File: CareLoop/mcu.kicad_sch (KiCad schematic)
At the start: 26 parts, among them J1_DEBUG1 Conn_01x04_Pin, U6 nRF52840-QFXX, Y1 32MHz, Y2 32.768kHz

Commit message: update PCB
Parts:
- C1, C2, C3, C4: JLCPCB Part#(optional) (none) -> C107034
- C10, C9: JLCPCB Part#(optional) (none) -> C62550
- C11, C7: JLCPCB Part#(optional) (none) -> C88945
- C12: JLCPCB Part#(optional) (none) -> C161494
- C5: JLCPCB Part#(optional) (none) -> C172832
- C6: JLCPCB Part#(optional) (none) -> C50388
- C8: JLCPCB Part#(optional) (none) -> C85925
- D3: JLCPCB Part#(optional) (none) -> C20608782
- J1_DEBUG1: footprint Connector_PinHeader_1.00mm:PinHeader_1x04_P1.00mm_Vertical -> Connector_PinHeader_2.00mm:PinHeader_1x04_P2.00mm_Vertical; now not fitted
- L1: JLCPCB Part#(optional) (none) -> C2043482
- L2: JLCPCB Part#(optional) (none) -> C2047913
- L5: JLCPCB Part#(optional) (none) -> C1035
- L6: JLCPCB Part#(optional) (none) -> C81212
- R1: JLCPCB Part#(optional) (none) -> C25531
- R2, R3: JLCPCB Part#(optional) (none) -> C22369185
- R4: JLCPCB Part#(optional) (none) -> C25097
- Reset_SW1: JLCPCB Part#(optional) (none) -> C2733655
- U6: JLCPCB Part#(optional) (none) -> C9900145907
- Y1: JLCPCB Part#(optional) (none) -> C252280
- Y2: JLCPCB Part#(optional) (none) -> C2449817
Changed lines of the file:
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@@
+			)
+		)
+		(property "JLCPCB Part#(optional)" "C161494"
+			(at 90.17 26.67 90)
+			(effects
+				(font
+					(size 1.27 1.27)
+				)
+				(hide yes)
 			)
 		)
@@
 			)
 		)
+		(property "JLCPCB Part#(optional)" "C9900145907"
+			(at 96.52 104.14 0)
+			(effects
+				(font
+					(size 1.27 1.27)
+				)
+				(hide yes)
+			)
+		)
 		(pin "35"
 		)
@@
 			)
 		)
+		(property "JLCPCB Part#(optional)" "C2449817"
+			(at 54.61 76.2 90)
+			(effects
+				(font
+					(size 1.27 1.27)
+				)
+				(hide yes)
+			)
+		)
 		(pin "1"
 		)
@@
 		(property "Description" "Resistor"
 			(at 45.72 127 0)
+			(effects
+				(font
+					(size 1.27 1.27)
+				)
+				(hide yes)
+			)
+		)
+		(property "JLCPCB Part#(optional)" "C25097"
+			(at 45.72 127 90)
 			(effects
 				(font
@@
 			)
 		)
+		(property "JLCPCB Part#(optional)" "C50388"
+			(at 160.02 100.33 0)
+			(effects
+				(font
+					(size 1.27 1.27)
+				)
+				(hide yes)
+			)
+		)
 		(pin "1"
 		)
@@
 		)
 		(property "Description" "Unpolarized capacitor, small symbol"
+			(at 139.7 55.88 0)
+			(effects
+				(font
+					(size 1.27 1.27)
+				)
+				(hide yes)
+			)
+		)
+		(property "JLCPCB Part#(optional)" "C62550"
 			(at 139.7 55.88 0)
 			(effects
@@
 			)
 		)
+		(property "JLCPCB Part#(optional)" "C81212"
+			(at 118.11 36.83 90)
+			(effects
+				(font
+					(size 1.27 1.27)
+				)
+				(hide yes)
+			)
+		)
 		(pin "2"
 		)
@@
 			)
 		)
+		(property "JLCPCB Part#(optional)" "C107034"
+			(at 45.72 80.01 90)
+			(effects
+				(font
+					(size 1.27 1.27)
+				)
+				(hide yes)
+			)
+		)
 		(pin "2"
 		)
@@
 			)
 		)
+		(property "JLCPCB Part#(optional)" "C2733655"
+			(at 148.59 147.32 0)
+			(effects
+				(font
+					(size 1.27 1.27)
+				)
+				(hide yes)
+			)
+		)
 		(pin "1"
 		)
@@
 		(property "Description" "Unpolarized capacitor, small symbol"
 			(at 45.72 72.39 0)
+			(effects
+				(font
+					(size 1.27 1.27)
+				)
+				(hide yes)
+			)
+		)
+		(property "JLCPCB Part#(optional)" "C107034"
+			(at 45.72 72.39 90)
 			(effects
 				(font
@@
 			)
 		)
+		(property "JLCPCB Part#(optional)" "C2047913"
+			(at 154.94 104.14 90)
+			(effects
+				(font
+					(size 1.27 1.27)
+				)
+				(hide yes)
+			)
+		)
 		(pin "2"
 		)
@@
 			)
 		)
+		(property "JLCPCB Part#(optional)" "C2043482"
+			(at 165.1 104.14 90)
+			(effects
+				(font
+					(size 1.27 1.27)
+				)
+				(hide yes)
+			)
+		)
 		(pin "2"
 		)
@@
 			)
 		)
+		(property "JLCPCB Part#(optional)" "C85925"
+			(at 144.78 68.58 0)
+			(effects
+				(font
+					(size 1.27 1.27)
+				)
+				(hide yes)
+			)
+		)
 		(pin "2"
 		)
@@
 		(property "Description" "Unpolarized capacitor, small symbol"
 			(at 45.72 64.77 0)
+			(effects
+				(font
+					(size 1.27 1.27)
+				)
+				(hide yes)
+			)
+		)
+		(property "JLCPCB Part#(optional)" "C107034"
+			(at 45.72 64.77 90)
 			(effects
 				(font
@@
 			)
 		)
+		(property "JLCPCB Part#(optional)" "C172832"
+			(at 149.86 100.33 0)
+			(effects
+				(font
+					(size 1.27 1.27)
+				)
+				(hide yes)
+			)
+		)
 		(pin "1"
 		)
@@
 			)
 		)
+		(property "JLCPCB Part#(optional)" "C88945"
+			(at 134.62 68.58 0)
+			(effects
+				(font
+					(size 1.27 1.27)
+				)
+				(hide yes)
+			)
+		)
 		(pin "2"
 		)
@@
 			)
 		)
+		(property "JLCPCB Part#(optional)" "C252280"
+			(at 57.15 60.96 90)
+			(effects
+				(font
+					(size 1.27 1.27)
+				)
+				(hide yes)
+			)
+		)
 		(pin "1"
 		)
@@
 			)
 		)
+		(property "JLCPCB Part#(optional)" "C88945"
+			(at 90.17 36.83 90)
+			(effects
+				(font
+					(size 1.27 1.27)
+				)
+				(hide yes)
+			)
+		)
 		(pin "2"
 		)
@@
 			)
 		)
+		(property "JLCPCB Part#(optional)" "C22369185"
+			(at 139.7 116.84 0)
+			(effects
+				(font
+					(size 1.27 1.27)
+				)
+				(hide yes)
+			)
+		)
 		(pin "1"
 		)
@@
 			)
 		)
+		(property "JLCPCB Part#(optional)" "C107034"
+			(at 45.72 57.15 90)
+			(effects
+				(font
+					(size 1.27 1.27)
+				)
+				(hide yes)
+			)
+		)
 		(pin "1"
 		)
@@
 		(in_bom yes)
 		(on_board yes)
-		(dnp no)
+		(dnp yes)
 		(property "Reference" "J1_DEBUG1"
 			(at 139.7 162.56 90)
@@
 			)
 		)
-		(property "Footprint" "Connector_PinHeader_1.00mm:PinHeader_1x04_P1.00mm_Vertical"
+		(property "Footprint" "Connector_PinHeader_2.00mm:PinHeader_1x04_P2.00mm_Vertical"
 			(at 138.43 160.02 0)
 			(effects
@@
 		(property "Description" "Generic connector, single row, 01x04, script generated"
 			(at 138.43 160.02 0)
+			(effects
+				(font
+					(size 1.27 1.27)
+				)
+				(hide yes)
+			)
+		)
+		(property "JLCPCB Part#(optional)" ""
+			(at 138.43 160.02 90)
 			(effects
 				(font
@@
 			)
 		)
+		(property "JLCPCB Part#(optional)" "C20608782"
+			(at 36.83 129.54 90)
+			(effects
+				(font
+					(size 1.27 1.27)
+				)
+				(hide yes)
+			)
+		)
 		(pin "2"
 		)
@@
 			)
 		)
+		(property "JLCPCB Part#(optional)" "C22369185"
+			(at 133.35 121.92 0)
+			(effects
+				(font
+					(size 1.27 1.27)
+				)
+				(hide yes)
+			)
+		)
 		(pin "1"
 		)
@@
 		(property "Description" "Resistor"
 			(at 158.75 144.78 0)
+			(effects
+				(font
+					(size 1.27 1.27)
+				)
+				(hide yes)
+			)
+		)
+		(property "JLCPCB Part#(optional)" "C25531"
+			(at 158.75 144.78 90)
 			(effects
 				(font
@@
 			)
 		)
+		(property "JLCPCB Part#(optional)" "C1035"
+			(at 102.87 36.83 90)
+			(effects
+				(font
+					(size 1.27 1.27)
+				)
+				(hide yes)
+			)
+		)
 		(pin "2"
 		)
@@
 			(at 130.81 50.8 0)
 			(effects
+				(font
+					(size 1.27 1.27)
+				)
+				(hide yes)
+			)
+		)
+		(property "JLCPCB Part#(optional)" "C62550"
+			(at 130.81 50.8 0)
+			(effects

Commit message: nordic review
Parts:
- C10: value 100p -> 100n; JLCPCB Part#(optional) C62550 -> C161404
- C12: JLCPCB Part#(optional) C161494 -> C161404
- C3, C4: value 12p -> 4p; JLCPCB Part#(optional) C107034 -> C384690
- R4: value 300 -> 800; JLCPCB Part#(optional) C25097 -> C11522
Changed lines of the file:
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@@
 			)
 		)
-		(property "JLCPCB Part#(optional)" "C161494"
+		(property "JLCPCB Part#(optional)" "C161404"
 			(at 90.17 26.67 90)
 			(effects
@@
 			)
 		)
-		(property "Value" "300"
+		(property "Value" "800"
 			(at 45.974 122.174 90)
 			(effects
@@
 			)
 		)
-		(property "JLCPCB Part#(optional)" "C25097"
+		(property "JLCPCB Part#(optional)" "C11522"
 			(at 45.72 127 90)
 			(effects
@@
 			)
 		)
-		(property "Value" "12p"
+		(property "Value" "4p"
 			(at 45.7136 76.2 90)
 			(effects
@@
 			)
 		)
-		(property "JLCPCB Part#(optional)" "C107034"
+		(property "JLCPCB Part#(optional)" "C384690"
 			(at 45.72 80.01 90)
 			(effects
@@
 			)
 		)
-		(property "Value" "12p"
+		(property "Value" "4p"
 			(at 45.466 69.596 90)
 			(effects
@@
 			)
 		)
-		(property "JLCPCB Part#(optional)" "C107034"
+		(property "JLCPCB Part#(optional)" "C384690"
 			(at 45.72 72.39 90)
 			(effects
@@
 			)
 		)
-		(property "Value" "100p"
+		(property "Value" "100n"
 			(at 133.35 52.0762 0)
 			(effects
@@
 			)
 		)
-		(property "JLCPCB Part#(optional)" "C62550"
+		(property "JLCPCB Part#(optional)" "C161404"
 			(at 130.81 50.8 0)
 			(effects

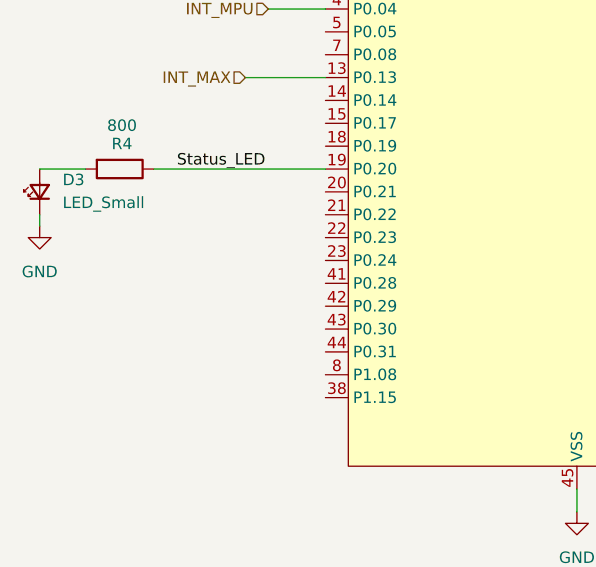
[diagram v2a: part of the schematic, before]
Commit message: update Voltagedevider
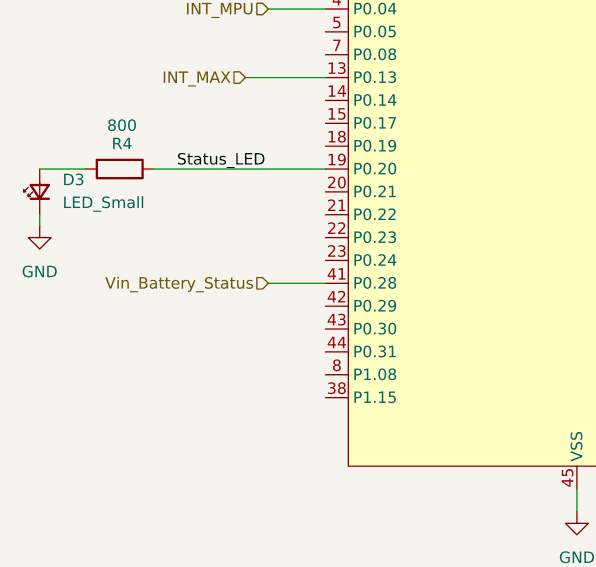
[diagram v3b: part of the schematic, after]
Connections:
- net Vin_Battery_Status: now reaches U6.41 (P0.28)
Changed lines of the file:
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@@
+	(wire
+		(pts
+			(xy 62.23 139.7) (xy 68.58 139.7)
+		)
+		(stroke
+			(width 0)
+			(type default)
+		)
+	)
 	(wire
 		(pts
@@
 		)
 	)
+	(hierarchical_label "Vin_Battery_Status"
+		(shape input)
+		(at 62.23 139.7 180)
+		(effects
+			(font
+				(size 1.27 1.27)
+			)
+			(justify right)
+		)
+	)
